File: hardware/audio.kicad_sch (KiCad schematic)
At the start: 33 parts, among them U1 PAM8406, U2 TPS79333-EP, U3 PCM5102

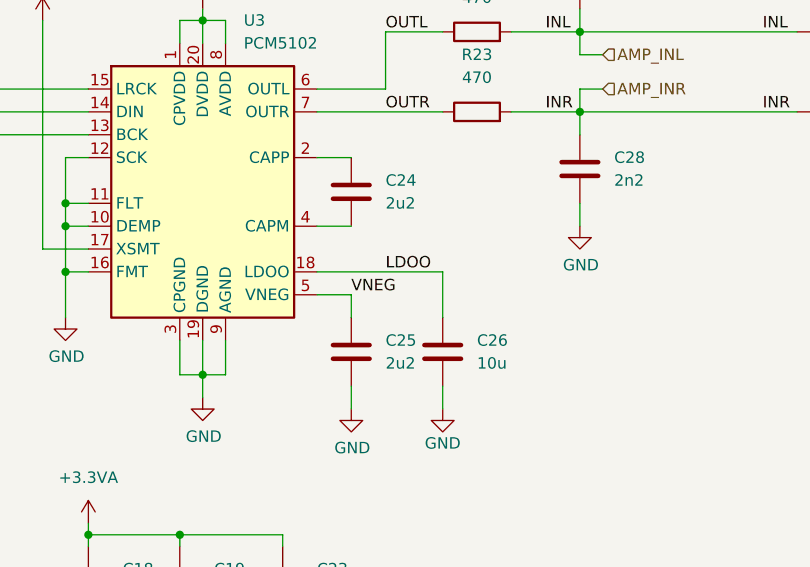
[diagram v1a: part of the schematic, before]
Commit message: Add BOM descriptions and JLC PCB LCSC part numbers. Generate gerber, drill and pick-and-place files.
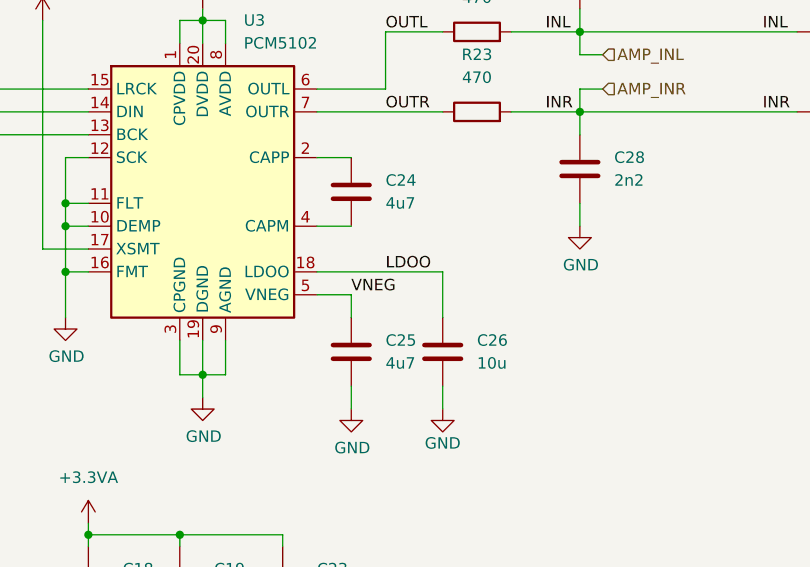
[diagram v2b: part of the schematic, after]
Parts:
- C10, C11, C12, C13: Comment (none) -> NP0 50V; LCSC (none) -> 0603N221J500CT
- C17, C20, C22: Comment (none) -> X7R 50V; LCSC (none) -> FN18X104K500PBG
- C18, C19, C23, C26, C4, C7: Comment (none) -> X7R 16V; LCSC (none) -> EMK316AB7106KL-T
- C2, C3, C5, C6: Comment (none) -> X7R 16V; LCSC (none) -> EMK107B7105KA-T
- C24, C25: value 2u2 -> 4u7; Comment (none) -> X5R 16V; LCSC (none) -> EMK107ABJ475KA-T
- C27, C28: Comment (none) -> NP0 50V; LCSC (none) -> 0603N222J500CT
- FB1, FB2, FB3, FB4: Comment (none) -> 120Ohm@100MHz 2A; LCSC (none) -> C354394
- R22, R23, R3, R4, R5: Comment (none) -> 5% 100ppm
- U1: Comment (none) -> PAM8406DR; LCSC (none) -> C86270
- U2: Comment (none) -> TPS79330DBVR; LCSC (none) -> C9840
- U3: Comment (none) -> PCM5102APWR; LCSC (none) -> C107671

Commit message: Smaller high value caps. Standard R/C footprints instead of hand solder.
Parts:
- C10, C11, C12, C13: footprint Capacitor_SMD:C_0603_1608Metric_Pad1.08x0.95mm_HandSolder -> Capacitor_SMD:C_0603_1608Metric; LCSC 0603N221J500CT -> (none)
- C17, C20, C22: footprint Capacitor_SMD:C_0603_1608Metric_Pad1.08x0.95mm_HandSolder -> Capacitor_SMD:C_0603_1608Metric; Comment X7R 50V -> X7R 10V; LCSC FN18X104K500PBG -> (none)
- C18, C19, C23, C26, C4, C7: footprint Capacitor_SMD:C_1210_3225Metric_Pad1.33x2.70mm_HandSolder -> Capacitor_SMD:C_0603_1608Metric; Comment X7R 16V -> X7R 10V; LCSC EMK316AB7106KL-T -> C32635
- C2, C3, C5, C6: footprint Capacitor_SMD:C_0603_1608Metric_Pad1.08x0.95mm_HandSolder -> Capacitor_SMD:C_0603_1608Metric; Comment X7R 16V -> X7R 10V; LCSC EMK107B7105KA-T -> (none)
- C24, C25: footprint Capacitor_SMD:C_0603_1608Metric_Pad1.08x0.95mm_HandSolder -> Capacitor_SMD:C_0603_1608Metric; Comment X5R 16V -> X7R 10V; LCSC EMK107ABJ475KA-T -> (none)
- C27, C28: footprint Capacitor_SMD:C_0603_1608Metric_Pad1.08x0.95mm_HandSolder -> Capacitor_SMD:C_0603_1608Metric; LCSC 0603N222J500CT -> (none)
- FB1, FB2, FB3, FB4, R22, R23, R3, R4, R5: footprint Resistor_SMD:R_0603_1608Metric_Pad0.98x0.95mm_HandSolder -> Resistor_SMD:R_0603_1608Metric

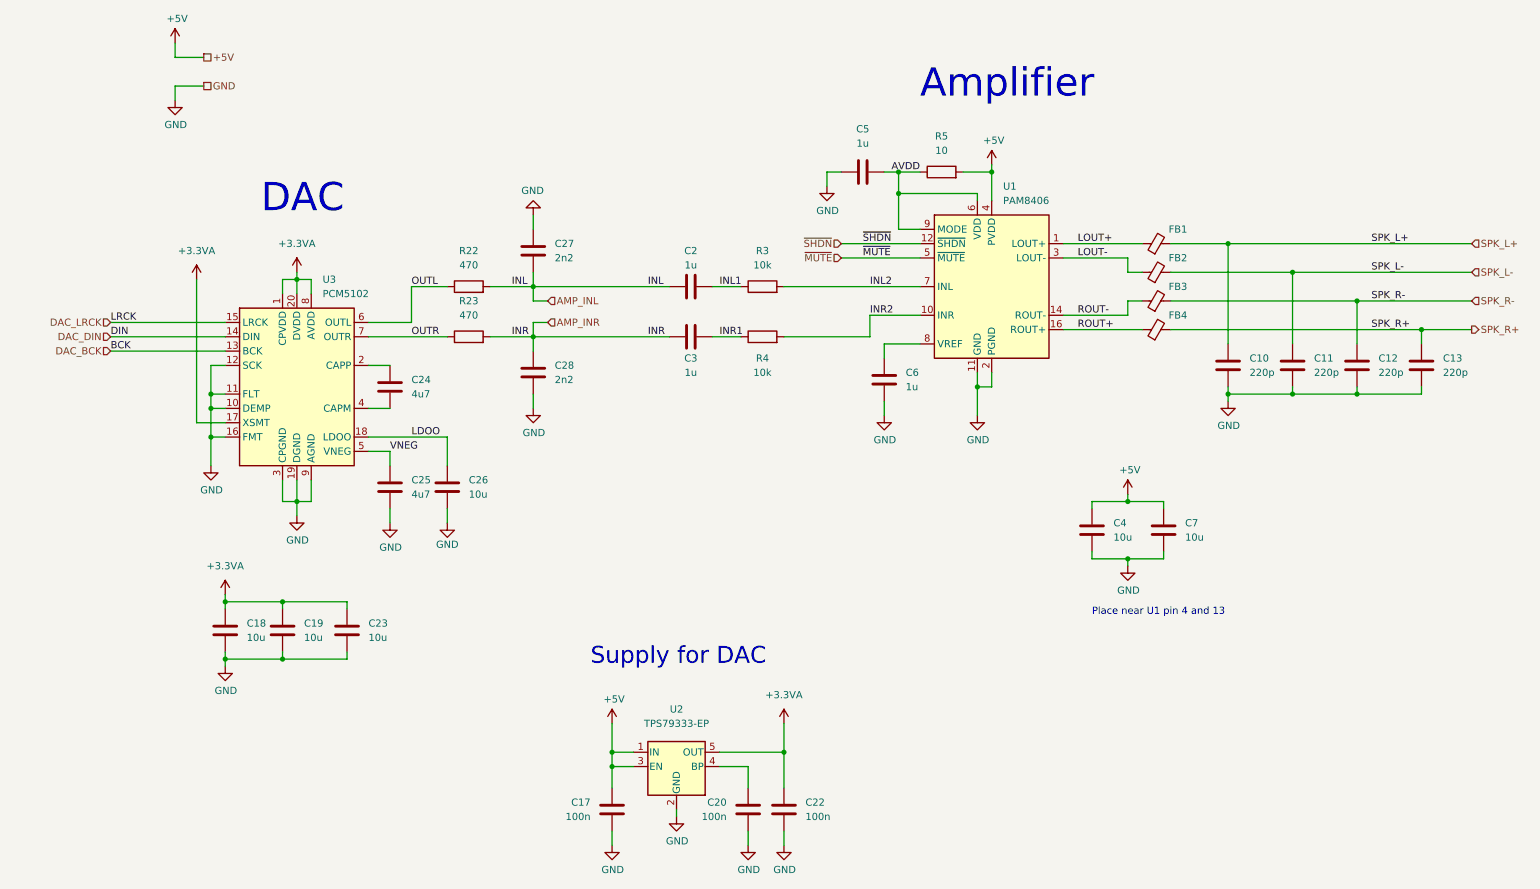
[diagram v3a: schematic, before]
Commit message: Move a lot of parts. Switch audio l/r (only in schematic). Next step: Apply in PCB.
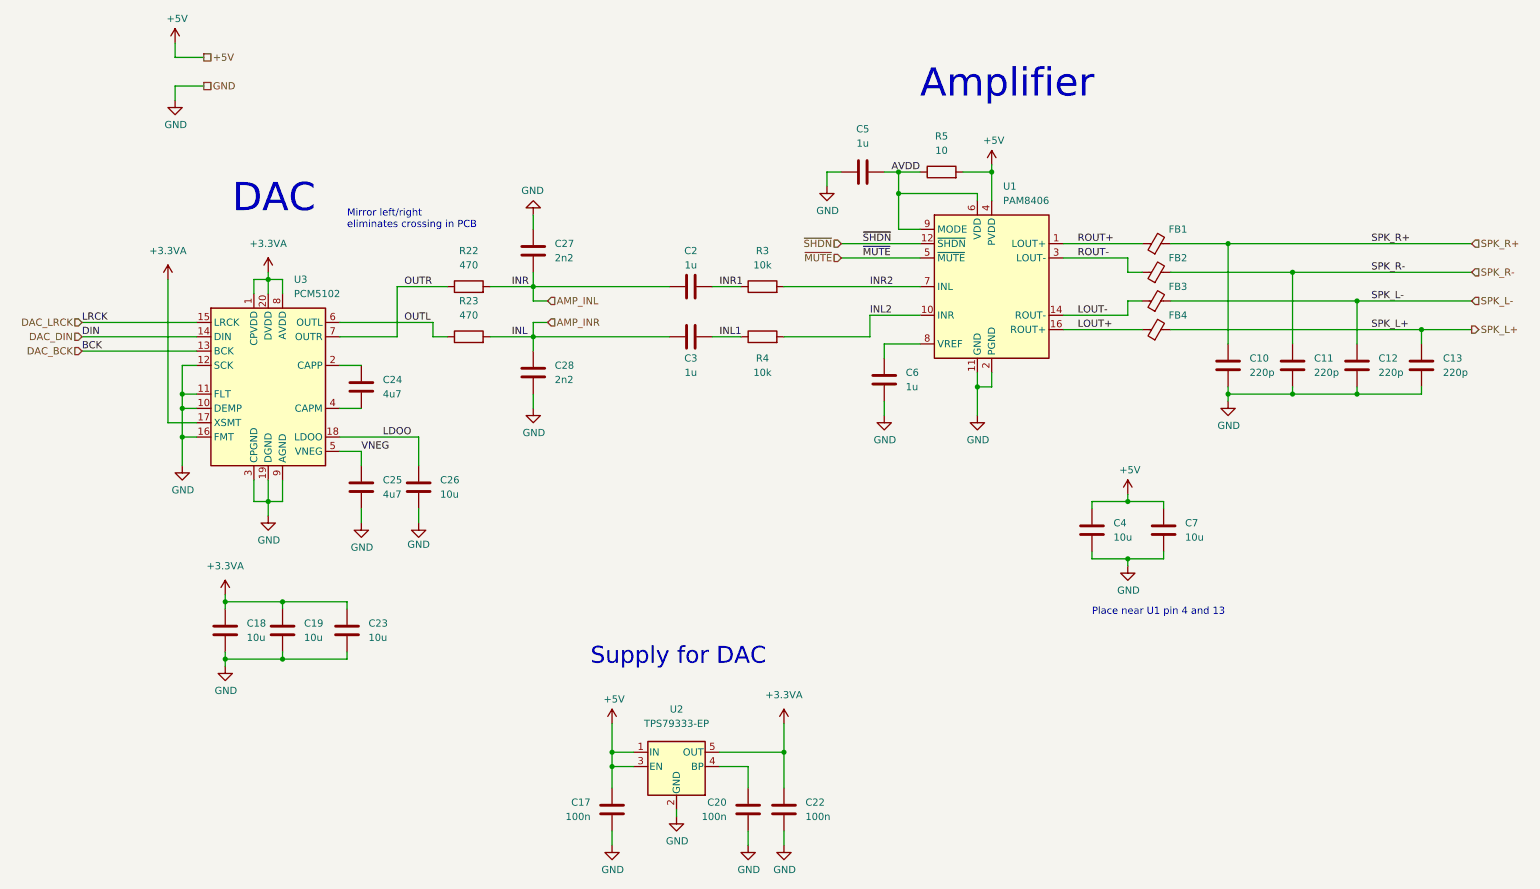
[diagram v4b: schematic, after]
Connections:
- net INL1: now also C3.2, R4.1; no longer C2.2, R3.1
- net INL2: now also R4.2, U1.10 (INR); no longer R3.2, U1.7 (INL)
- net INR1: now also C2.2, R3.1; no longer C3.2, R4.1
- net INR2: now also R3.2, U1.7 (INL); no longer R4.2, U1.10 (INR)
- net LOUT+: now also FB4.1, U1.16 (ROUT+); no longer FB1.1, U1.1 (LOUT+)
- net LOUT-: now also FB3.1, U1.14 (ROUT-); no longer FB2.1, U1.3 (LOUT-)
- net OUTL: now also R23.1; no longer R22.1
- net OUTR: now also R22.1; no longer R23.1
- net ROUT+: now also FB1.1, U1.1 (LOUT+); no longer FB4.1, U1.16 (ROUT+)
- net ROUT-: now also FB2.1, U1.3 (LOUT-); no longer FB3.1, U1.14 (ROUT-)
- net SPK_L+: now also C13.1, FB4.2; no longer C10.1, FB1.2
- net SPK_L-: now also C12.1, FB3.2; no longer C11.1, FB2.2
- net SPK_R+: now also C10.1, FB1.2; no longer C13.1, FB4.2
- net SPK_R-: now also C11.1, FB2.2; no longer C12.1, FB3.2
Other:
- note added: "Mirror left/right eliminates crossing in PCB"
- moved on the sheet: C24, C25, C26, U3

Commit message: Moved DAC. Replace pin headers with single row SMD ones (compatible with RC522/display PCBs to connect).
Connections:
- net AMP_INL: now also C28.1, C3.1, R23.2; no longer C2.1, C27.2, R22.2
- net AMP_INR: now also C2.1, C27.2, R22.2; no longer C28.1, C3.1, R23.2
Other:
- note added: "Mirroring left/right eliminates crossing in PCB"
- note removed: "Mirror left/right eliminates crossing in PCB"

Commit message: Size 0805 for 10uF capacitors.
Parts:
- C18, C19, C23, C26, C4, C7: footprint Capacitor_SMD:C_0603_1608Metric -> Capacitor_SMD:C_0805_2012Metric; LCSC C32635 -> (none)
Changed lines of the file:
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@@
       (effects (font (size 1.27 1.27)) (justify left))
     )
-    (property "Footprint" "Capacitor_SMD:C_0603_1608Metric" (id 2) (at 50.4952 132.08 0)
+    (property "Footprint" "Capacitor_SMD:C_0805_2012Metric" (id 2) (at 50.4952 132.08 0)
       (effects (font (size 1.27 1.27)) hide)
     )
@@
       (effects (font (size 1.27 1.27)) hide)
     )
-    (property "LCSC" "C32635" (id 5) (at 49.53 128.27 0)
+    (property "LCSC" "" (id 5) (at 49.53 128.27 0)
       (effects (font (size 1.27 1.27)) hide)
     )
@@
       (effects (font (size 1.27 1.27)) (justify left))
     )
-    (property "Footprint" "Capacitor_SMD:C_0603_1608Metric" (id 2) (at 204.1652 114.3 0)
+    (property "Footprint" "Capacitor_SMD:C_0805_2012Metric" (id 2) (at 204.1652 114.3 0)
       (effects (font (size 1.27 1.27)) hide)
     )
@@
       (effects (font (size 1.27 1.27)) hide)
     )
-    (property "LCSC" "C32635" (id 5) (at 203.2 110.49 0)
+    (property "LCSC" "" (id 5) (at 203.2 110.49 0)
       (effects (font (size 1.27 1.27)) hide)
     )
@@
       (effects (font (size 1.27 1.27)) (justify left))
     )
-    (property "Footprint" "Capacitor_SMD:C_0603_1608Metric" (id 2) (at 72.0852 132.08 0)
+    (property "Footprint" "Capacitor_SMD:C_0805_2012Metric" (id 2) (at 72.0852 132.08 0)
       (effects (font (size 1.27 1.27)) hide)
     )
@@
       (effects (font (size 1.27 1.27)) hide)
     )
-    (property "LCSC" "C32635" (id 5) (at 71.12 128.27 0)
+    (property "LCSC" "" (id 5) (at 71.12 128.27 0)
       (effects (font (size 1.27 1.27)) hide)
     )
@@
       (effects (font (size 1.27 1.27)) (justify left))
     )
-    (property "Footprint" "Capacitor_SMD:C_0603_1608Metric" (id 2) (at 216.8652 114.3 0)
+    (property "Footprint" "Capacitor_SMD:C_0805_2012Metric" (id 2) (at 216.8652 114.3 0)
       (effects (font (size 1.27 1.27)) hide)
     )
@@
       (effects (font (size 1.27 1.27)) hide)
     )
-    (property "LCSC" "C32635" (id 5) (at 215.9 110.49 0)
+    (property "LCSC" "" (id 5) (at 215.9 110.49 0)
       (effects (font (size 1.27 1.27)) hide)
     )
@@
       (effects (font (size 1.27 1.27)) (justify left))
     )
-    (property "Footprint" "Capacitor_SMD:C_0603_1608Metric" (id 2) (at 60.6552 132.08 0)
+    (property "Footprint" "Capacitor_SMD:C_0805_2012Metric" (id 2) (at 60.6552 132.08 0)
       (effects (font (size 1.27 1.27)) hide)
     )
@@
       (effects (font (size 1.27 1.27)) hide)
     )
-    (property "LCSC" "C32635" (id 5) (at 59.69 128.27 0)
+    (property "LCSC" "" (id 5) (at 59.69 128.27 0)
       (effects (font (size 1.27 1.27)) hide)
     )
@@
       (effects (font (size 1.27 1.27)) (justify left))
     )
-    (property "Footprint" "Capacitor_SMD:C_0603_1608Metric" (id 2) (at 84.7852 106.68 0)
+    (property "Footprint" "Capacitor_SMD:C_0805_2012Metric" (id 2) (at 84.7852 106.68 0)
       (effects (font (size 1.27 1.27)) hide)
     )
@@
       (effects (font (size 1.27 1.27)) hide)
     )
-    (property "LCSC" "C32635" (id 5) (at 83.82 102.87 0)
-      (effects (font (size 1.27 1.27)) hide)
-    )
+    (property "LCSC" "" (id 5) (at 83.82 102.87 0)
+      (effects (font (size 1.27 1.27)) hide)
+    )

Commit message: Fix all ERC warnings. Replace 4u7 capacitor in cut-off circuit by 100 nF cap and 10 kOhm in series to reduce stress on Raspi GPIO.
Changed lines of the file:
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@@
+    (stroke (width 0) (type default) (color 0 0 0 0))
+  )
+  (wire (pts (xy 168.91 45.72) (xy 168.91 46.99))
     (stroke (width 0) (type default) (color 0 0 0 0))
   )
@@
   )
   (wire (pts (xy 49.53 124.46) (xy 49.53 123.19))
+    (stroke (width 0) (type default) (color 0 0 0 0))
+  )
+  (wire (pts (xy 113.03 149.86) (xy 118.11 149.86))
     (stroke (width 0) (type default) (color 0 0 0 0))
   )
@@
     (effects (font (size 1.27 1.27)) (justify left bottom))
   )
-  (label "SPK_R-" (at 252.73 64.77 0)
-    (effects (font (size 1.27 1.27)) (justify left bottom))
-  )
-  (label "INL" (at 116.84 76.2 0)
-    (effects (font (size 1.27 1.27)) (justify left bottom))
-  )
-  (label "AVDD" (at 167.64 46.99 0)
-    (effects (font (size 1.27 1.27)) (justify left bottom))
-  )
-  (label "BCK" (at 24.13 78.74 0)
+  (label "AVDD" (at 171.45 50.8 0)
     (effects (font (size 1.27 1.27)) (justify left bottom))
   )
@@
     (effects (font (size 1.27 1.27)) (justify left bottom))
   )
-  (label "SPK_R+" (at 252.73 59.69 0)
-    (effects (font (size 1.27 1.27)) (justify left bottom))
-  )
   (label "VNEG" (at 73.66 96.52 0)
     (effects (font (size 1.27 1.27)) (justify left bottom))
@@
     (effects (font (size 1.27 1.27)) (justify left bottom))
   )
-  (label "DIN" (at 24.13 76.2 0)
-    (effects (font (size 1.27 1.27)) (justify left bottom))
-  )
-  (label "INR" (at 116.84 67.31 0)
-    (effects (font (size 1.27 1.27)) (justify left bottom))
-  )
-  (label "SPK_L+" (at 252.73 74.93 0)
-    (effects (font (size 1.27 1.27)) (justify left bottom))
-  )
   (label "OUTL" (at 81.28 73.66 0)
     (effects (font (size 1.27 1.27)) (justify left bottom))
   )
-  (label "SPK_L-" (at 252.73 69.85 0)
-    (effects (font (size 1.27 1.27)) (justify left bottom))
-  )
-  (label "LRCK" (at 24.13 73.66 0)
-    (effects (font (size 1.27 1.27)) (justify left bottom))
-  )
   (label "ROUT+" (at 200.66 59.69 0)
     (effects (font (size 1.27 1.27)) (justify left bottom))
@@
     (effects (font (size 1.27 1.27)) (justify left bottom))
   )
-  (hierarchical_label "SPK_L-" (shape input) (at 270.51 69.85 0)
+  (hierarchical_label "SPK_L-" (shape output) (at 270.51 69.85 0)
     (effects (font (size 1.27 1.27)) (justify left))
   )
-  (hierarchical_label "GND" (shape passive) (at 45.72 31.75 0)
+  (hierarchical_label "GND" (shape input) (at 45.72 31.75 0)
     (effects (font (size 1.27 1.27)) (justify left))
   )
@@
     (effects (font (size 1.27 1.27)) (justify right))
   )
-  (hierarchical_label "+5V" (shape passive) (at 45.72 26.67 0)
+  (hierarchical_label "+5V" (shape input) (at 45.72 26.67 0)
     (effects (font (size 1.27 1.27)) (justify left))
   )
@@
     (effects (font (size 1.27 1.27)) (justify right))
   )
-  (hierarchical_label "SPK_R-" (shape input) (at 270.51 64.77 0)
+  (hierarchical_label "SPK_R-" (shape output) (at 270.51 64.77 0)
     (effects (font (size 1.27 1.27)) (justify left))
   )
@@
     (effects (font (size 1.27 1.27)) (justify right))
   )
-  (hierarchical_label "SPK_R+" (shape input) (at 270.51 59.69 0)
+  (hierarchical_label "SPK_R+" (shape output) (at 270.51 59.69 0)
     (effects (font (size 1.27 1.27)) (justify left))
   )
@@
     (pin "1")
   )
+  (symbol (lib_id "power:PWR_FLAG") (at 113.03 149.86 90) (unit 1)
+    (in_bom yes) (on_board yes) (fields_autoplaced)
+    (property "Reference" "#FLG03" (id 0) (at 111.125 149.86 0)
+      (effects (font (size 1.27 1.27)) hide)
+    )
+    (property "Value" "PWR_FLAG" (id 1) (at 111.76 146.05 90))
+    (property "Footprint" "" (id 2) (at 113.03 149.86 0)
+      (effects (font (size 1.27 1.27)) hide)
+    )
+    (property "Datasheet" "~" (id 3) (at 113.03 149.86 0)
+      (effects (font (size 1.27 1.27)) hide)
+    )
+    (pin "1")
+  )
   (symbol (lib_id "Device:C") (at 142.24 160.02 0) (mirror x) (unit 1)
     (in_bom yes) (on_board yes) (fields_autoplaced)
@@
     (pin "1")
     (pin "2")
+  )
+  (symbol (lib_id "power:+5V") (at 118.11 144.78 0) (unit 1)
+    (in_bom yes) (on_board yes)
+    (property "Reference" "#PWR0130" (id 0) (at 118.11 148.59 0)
+      (effects (font (size 1.27 1.27)) hide)
+    )
+    (property "Value" "+5V" (id 1) (at 118.4783 140.4556 0))
+    (property "Footprint" "" (id 2) (at 118.11 144.78 0))
+    (property "Datasheet" "" (id 3) (at 118.11 144.78 0))
+    (pin "1")
   )
   (symbol (lib_id "power:+3.3VA") (at 57.15 64.77 0) (unit 1)
@@
     (pin "2")
   )
+  (symbol (lib_id "power:PWR_FLAG") (at 168.91 45.72 0) (unit 1)
+    (in_bom yes) (on_board yes) (fields_autoplaced)
+    (property "Reference" "#FLG0102" (id 0) (at 168.91 43.815 0)
+      (effects (font (size 1.27 1.27)) hide)
+    )
+    (property "Value" "PWR_FLAG" (id 1) (at 168.91 40.64 0))
+    (property "Footprint" "" (id 2) (at 168.91 45.72 0)
+      (effects (font (size 1.27 1.27)) hide)
+    )
+    (property "Datasheet" "~" (id 3) (at 168.91 45.72 0)
+      (effects (font (size 1.27 1.27)) hide)
+    )
+    (pin "1")
+  )
   (symbol (lib_id "Device:R") (at 92.71 76.2 90) (unit 1)
     (in_bom yes) (on_board yes) (fields_autoplaced)
@@
     (pin "1")
   )
-  (symbol (lib_id "power:+5V") (at 118.11 144.78 0) (unit 1)
-    (in_bom yes) (on_board yes)
-    (property "Reference" "#PWR0130" (id 0) (at 118.11 148.59 0)
-      (effects (font (size 1.27 1.27)) hide)
-    )
-    (property "Value" "+5V" (id 1) (at 118.4783 140.4556 0))
-    (property "Footprint" "" (id 2) (at 118.11 144.78 0))
-    (property "Datasheet" "" (id 3) (at 118.11 144.78 0))
-    (pin "1")
-  )
